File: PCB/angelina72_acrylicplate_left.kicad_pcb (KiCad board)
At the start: 2 copper layers, 162.3 x 124.6 mm, 24 parts, among them U1 ProMicro

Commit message: Update acrylic case
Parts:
- added REF**: Outline_MXCherry_1u, angelina72:Outline_MXCherry_1u, F.Cu at (185.3, 148.6)
- moved REF** 34.5 mm to (160.3, 142.8)
- moved REF** 4.29 mm to (56.2, 46.5)
- moved REF** 4.29 mm to (199.7, 160.7)
- moved REF** 4.29 mm to (56.2, 122.5)
- moved REF** 4.29 mm to (193.7, 40.3)

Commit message: アクリル積層ケースの再設計(左手)
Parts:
- removed the REF** at (160.3, 142.8)
- removed the REF** at (223.0, 62.0)
- removed the REF** at (63.3, 34.6)
- removed the REF** at (216.9, 96.9)
- removed the REF** at (214.5, 110.5)
- removed the REF** at (185.3, 148.6)
- added REF**: M2_AcrylicHole, angelina72:M2_AcrylicHole, F.Cu at (186.8, 166.0)
- added REF**: MJ-19_3.5mm, angelina72:MJ-19_3.5mm, F.Cu at (222.0, 105.8)
- added REF**: M2_AcrylicHole, angelina72:M2_AcrylicHole, F.Cu at (126.0, 34.9)
- added REF**: M2_AcrylicHole, angelina72:M2_AcrylicHole, F.Cu at (62.7, 33.9)
- added REF**: M2_AcrylicHole, angelina72:M2_AcrylicHole, F.Cu at (209.2, 139.4)
- added REF**: M2_AcrylicHole, angelina72:M2_AcrylicHole, F.Cu at (159.9, 143.4)
- added REF**: M2_AcrylicHole, angelina72:M2_AcrylicHole, F.Cu at (214.2, 112.1)
- added REF**: M2_AcrylicHole, angelina72:M2_AcrylicHole, F.Cu at (216.8, 97.1)
- added REF**: M2_AcrylicHole, angelina72:M2_AcrylicHole, F.Cu at (111.3, 134.9)
- added REF**: M2_AcrylicHole, angelina72:M2_AcrylicHole, F.Cu at (222.9, 61.7)
- added SW10: KEY_SWITCH, angelina72:Outline_MXCherry_1u, F.Cu at (94.9, 46.3)
- added SW11: KEY_SWITCH, angelina72:Outline_MXCherry_1u, F.Cu at (100.8, 65.3)
- added SW12: KEY_SWITCH, angelina72:Outline_MXCherry_1u, F.Cu at (97.7, 84.4)
- added SW13: KEY_SWITCH, angelina72:Outline_MXCherry_1u, F.Cu at (103.7, 103.4)
- added SW14: KEY_SWITCH, angelina72:Outline_MXCherry_1u, F.Cu at (98.9, 122.5)
- added SW15: KEY_SWITCH, angelina72:Outline_MXCherry_1u, F.Cu at (113.9, 45.6)
- added SW16: KEY_SWITCH, angelina72:Outline_MXCherry_1u, F.Cu at (121.5, 66.1)
- added SW17: KEY_SWITCH, angelina72:Outline_MXCherry_1u, F.Cu at (118.2, 84.8)
- added SW18: KEY_SWITCH, angelina72:Outline_MXCherry_1u, F.Cu at (124.3, 105.2)
- added SW19: KEY_SWITCH, angelina72:Outline_MXCherry_1.25u, F.Cu at (123.3, 124.4)
- added SW20: KEY_SWITCH, angelina72:Outline_MXCherry_1u, F.Cu at (134.2, 49.0)
- added SW21: KEY_SWITCH, angelina72:Outline_MXCherry_1u, F.Cu at (140.3, 69.4)
- added SW22: KEY_SWITCH, angelina72:Outline_MXCherry_1u, F.Cu at (136.9, 88.1)
- added SW23: KEY_SWITCH, angelina72:Outline_MXCherry_1u, F.Cu at (143.0, 108.5)
- added SW24: KEY_SWITCH, angelina72:Outline_MXCherry_1.25u, F.Cu at (146.7, 128.5)
- added SW25: KEY_SWITCH, angelina72:Outline_MXCherry_1u, F.Cu at (152.9, 52.3)
- added SW26: KEY_SWITCH, angelina72:Outline_MXCherry_1u, F.Cu at (159.0, 72.7)
- added SW27: KEY_SWITCH, angelina72:Outline_MXCherry_1u, F.Cu at (155.7, 91.4)
- added SW28: KEY_SWITCH, angelina72:Outline_MXCherry_1u, F.Cu at (161.8, 111.8)
- added SW29: KEY_SWITCH, angelina72:Outline_MXCherry_1u, F.Cu at (171.7, 55.6)
- added SW30: KEY_SWITCH, angelina72:Outline_MXCherry_1u, F.Cu at (177.8, 76.0)
- added SW31: KEY_SWITCH, angelina72:Outline_MXCherry_1u, F.Cu at (174.5, 94.7)
- added SW32: KEY_SWITCH, angelina72:Outline_MXCherry_1u, F.Cu at (180.5, 115.2)
- added SW33: KEY_SWITCH, angelina72:Outline_MXCherry_1u, F.Cu at (170.7, 136.3)
- added SW34: KEY_SWITCH, angelina72:Outline_MXCherry_1u, F.Cu at (190.5, 58.9)
- added SW35: KEY_SWITCH, angelina72:Outline_MXCherry_1u, F.Cu at (197.5, 134.0)
- added SW36: KEY_SWITCH, angelina72:Outline_MXCherry_1u, F.Cu at (185.3, 148.5)
- added SW5: KEY_SWITCH, angelina72:Outline_MXCherry_1u, F.Cu at (75.8, 46.3)
- added SW6: KEY_SWITCH, angelina72:Outline_MXCherry_1u, F.Cu at (81.8, 65.3)
- added SW7: KEY_SWITCH, angelina72:Outline_MXCherry_1u, F.Cu at (78.7, 84.4)
- added SW8: KEY_SWITCH, angelina72:Outline_MXCherry_1u, F.Cu at (84.6, 103.4)
- added SW9: KEY_SWITCH, angelina72:Outline_MXCherry_1.25u, F.Cu at (77.5, 122.5)
- moved REF** 0.98 mm to (193.7, 39.4)
- moved REF** 0.98 mm to (200.6, 161.1)
- moved REF** 0.93 mm to (62.7, 134.9)
- moved REF** 0.87 mm to (55.4, 46.3)
- moved REF** 0.83 mm to (55.4, 122.5)
- moved REF** 0.75 mm to (204.3, 48.7)
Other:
- board text added: "F.Adhes = bottom Eco1.User = inner inner Eco2.User = inner outer B.Adhes = top"

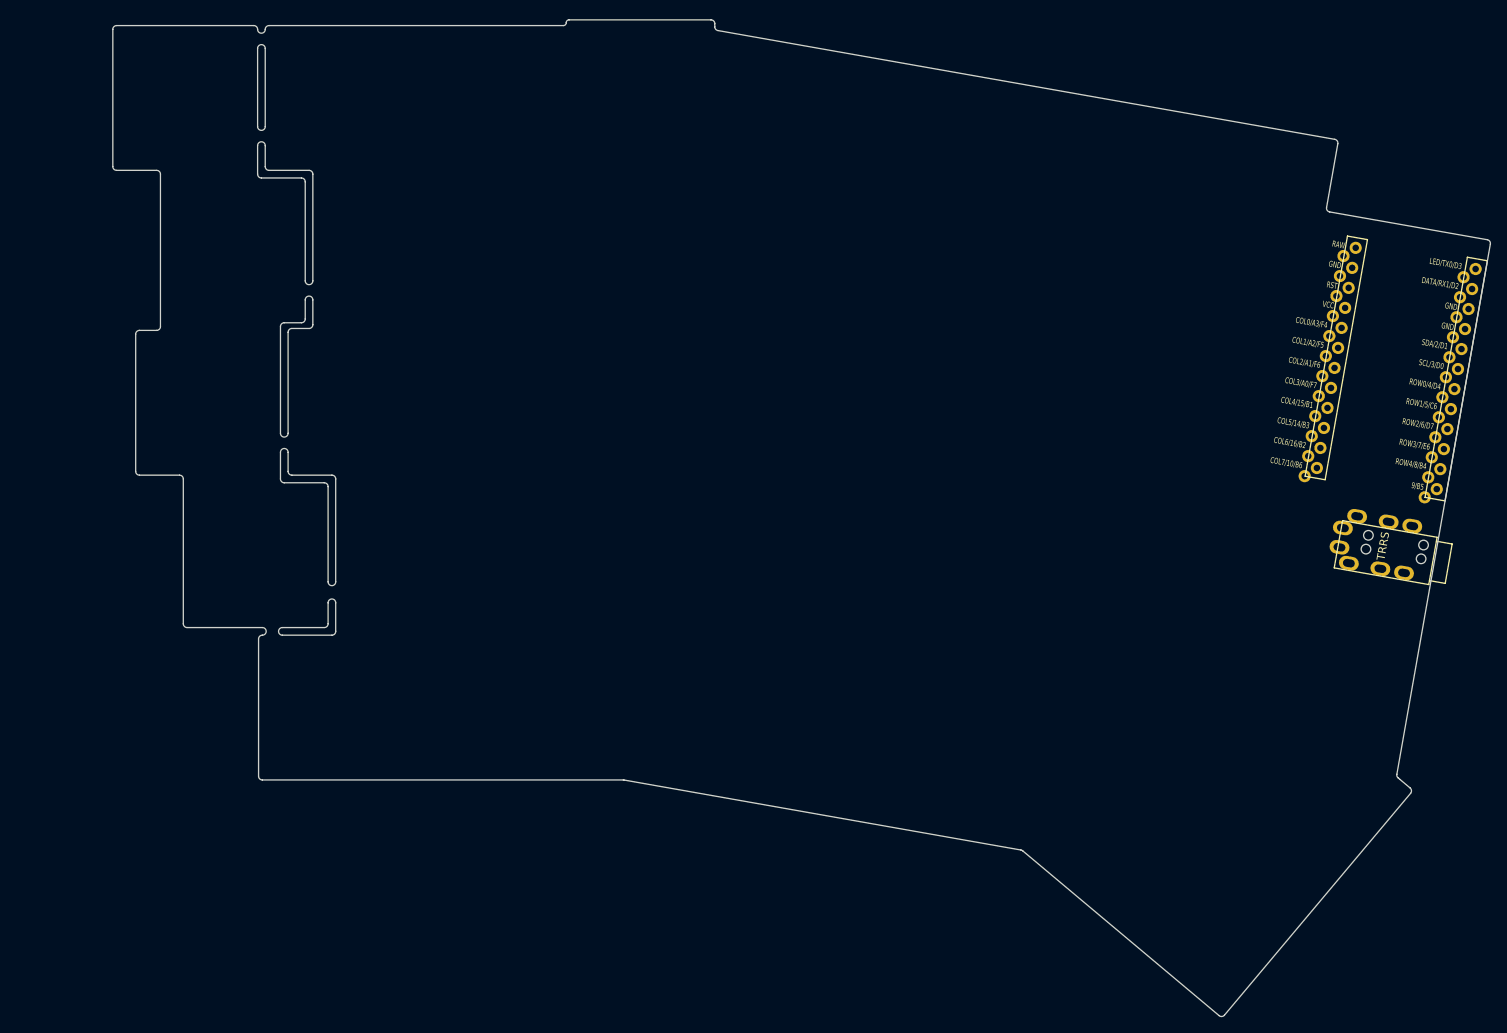
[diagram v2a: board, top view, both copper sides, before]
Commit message: PCBの空きレイヤーでscad用のポリゴンを書いた
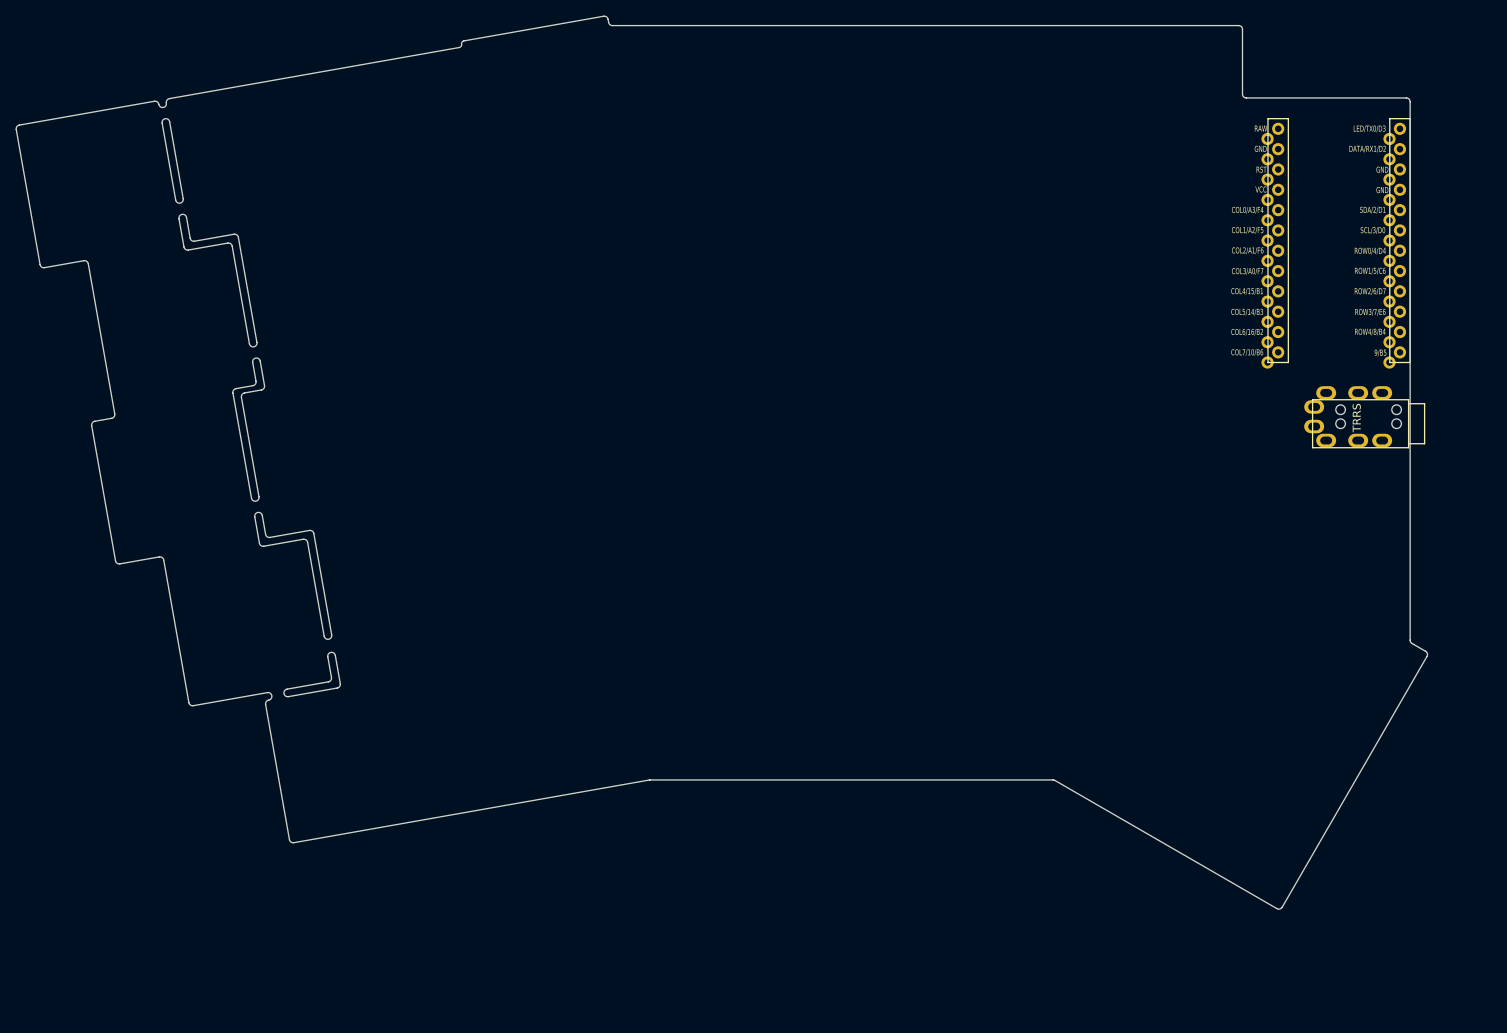
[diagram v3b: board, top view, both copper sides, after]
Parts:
- removed the REF** at (205.9, 123.3)
- removed the REF** at (206.8, 110.1)
- removed the REF** at (196.0, 100.2)
- moved REF** 21.1 mm to (212.3, 43.4), turned to 0 degrees
- moved REF** 19.4 mm to (191.8, 33.9), turned to 0 degrees
- moved REF** 19.0 mm to (179.7, 26.5), turned to 0 degrees
- moved REF** 19.0 mm to (219.1, 87.0), turned to 0 degrees
- moved REF** 18.3 mm to (212.5, 79.4), turned to 270 degrees
- moved REF** 17.6 mm to (212.5, 94.6), turned to 0 degrees
- moved U1 17.5 mm to (201.0, 64.6), turned to 0 degrees
- moved REF** 17.4 mm to (207.6, 145.2), turned to 240 degrees
- moved REF** 17.3 mm to (212.3, 122.4), turned to 150 degrees
- moved SW34 16.4 mm to (179.9, 46.3), turned to 0 degrees
- moved J* 16.4 mm to (203.7, 87.0), turned to 270 degrees
- moved REF** 16.4 mm to (49.8, 43.9), turned to 280 degrees
- moved REF** 15.8 mm to (194.9, 152.4), turned to 240 degrees
- moved REF** 15.4 mm to (44.7, 57.3), turned to 100 degrees
- moved SW35 15.1 mm to (199.9, 119.0), turned to 330 degrees
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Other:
- board size 162.3 x 124.6 mm -> 176.4 x 111.6 mm
